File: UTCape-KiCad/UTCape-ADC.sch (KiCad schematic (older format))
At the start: 3 parts

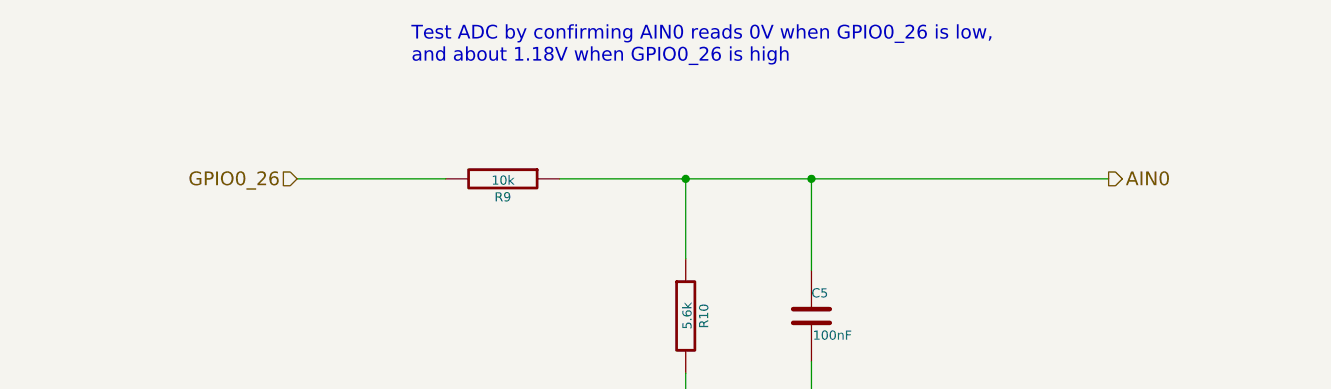
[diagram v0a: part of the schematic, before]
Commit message: layed out PCB, some minor wiring changes for layout
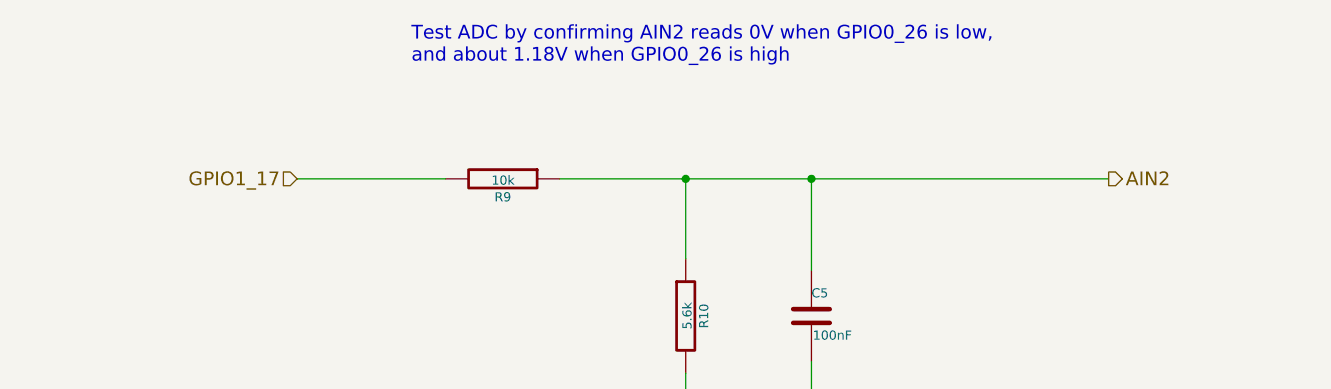
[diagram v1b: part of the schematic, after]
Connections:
- net AIN0 renamed AIN2
- net GPIO0_26 renamed GPIO1_17
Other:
- note added: "Test ADC by confirming AIN2 reads 0V when GPIO0_26 is low,\nand about 1.18V when GPIO0_26 is high"
- note removed: "Test ADC by confirming AIN0 reads 0V when GPIO0_26 is low,\nand about 1.18V when GPIO0_26 is high"
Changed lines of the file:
@@
 LIBS:contrib
 LIBS:valves
+LIBS:beagleboneblack
 LIBS:GrayCatLabs
-LIBS:BeagleBoneBlack
 LIBS:UTCape-cache
 EELAYER 27 0
@@
 1.
 Text HLabel 7650 3500 2    60   Output ~ 0
-AIN0
+AIN2
 Text HLabel 4100 3500 0    60   Input ~ 0
-GPIO0_26
+GPIO1_17
 $Comp
 L R R9
@@
 Connection ~ 5800 4550
 Text Notes 4600 3000 0    60   ~ 0
-Test ADC by confirming AIN0 reads 0V when GPIO0_26 is low,\nand about 1.18V when GPIO0_26 is high
+Test ADC by confirming AIN2 reads 0V when GPIO0_26 is low,\nand about 1.18V when GPIO0_26 is high
 $Bitmap
 Pos 6300 7500
@@
 03 43 83 61 8C 09 03 03 03 03 43 83 61 8C 09 03 03 03 03 43 83 61 8C 09 03 03 03 03 43 83 61 03
 60 D2 64 32 30 30 30 30 34 84 CF 1C 00 A9 00 9C 01 A8 8B 59 19 06 06 06 06 06 E9 E3 33 80 C5 FF
-07 47 25 A5 D2 E9 03 52 D8 00 00 00 00 49 45 4E 44 AE 42 60 82 76 $EndBitmap
+07 47 25 A5 D2 E9 03 52 D8 00 00 00 00 49 45 4E 44 AE 42 60 82 4A $EndBitmap
 EndData
 $EndBitmap
